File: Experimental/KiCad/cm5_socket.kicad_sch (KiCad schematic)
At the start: 23 parts, among them Q1 2N7002, X1 1-2199230-6

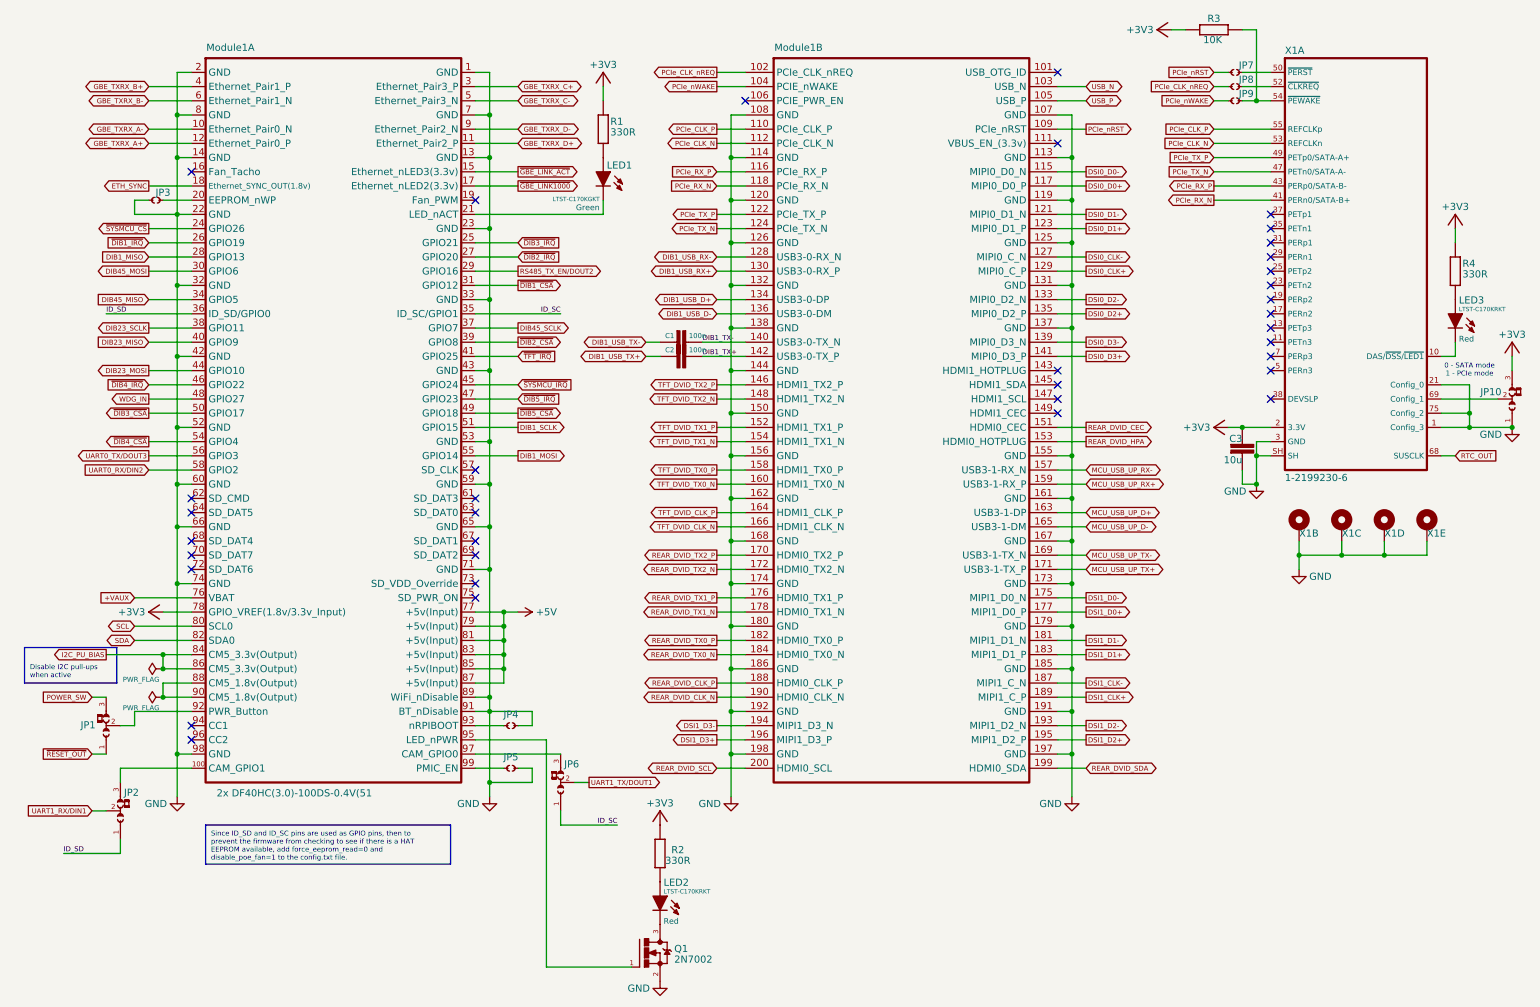
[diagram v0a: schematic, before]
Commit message: BOM update, small changes
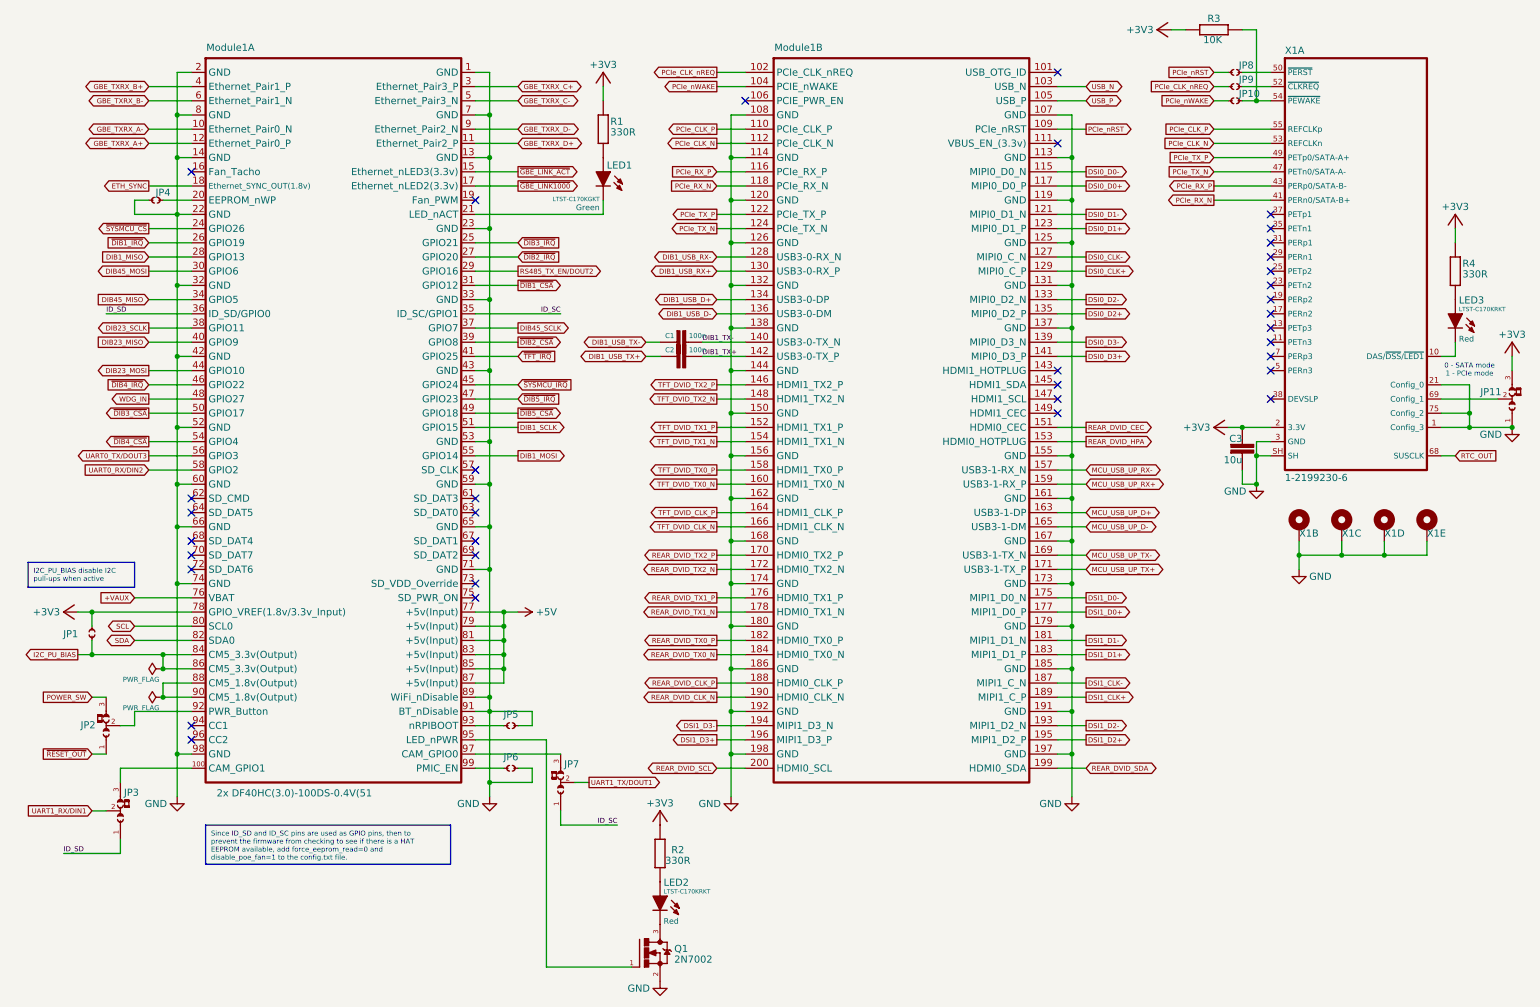
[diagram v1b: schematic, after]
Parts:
- added JP1: ~, PCM_EEZ_connectors:M22-2010246, symbol PCM_EEZ_unsorted:JP2 open
- renumbered JP9 to JP10, JP10 to JP11, JP1 to JP2, JP2 to JP3, JP3 to JP4, JP4 to JP5, JP5 to JP6, JP6 to JP7, JP7 to JP8, JP8 to JP9
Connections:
- net +3V3: now also JP1.2
- net I2C_PU_BIAS: now also JP1.1
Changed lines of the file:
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@@
 	(title_block
 		(title "BB3+ test mainboard")
-		(date "2025-10-11")
+		(date "2025-10-12")
 		(rev "r1B1")
 		(company "Envox d.o.o.")
@@
 		)
 	)
-	(text_box "Disable I2C pull-ups\nwhen active"
+	(text_box "I2C_PU_BIAS disable I2C\npull-ups when active"
 		(exclude_from_sim no)
-		(at 13.335 130.81 0)
-		(size 16.51 6.35)
+		(at 13.97 115.57 0)
+		(size 19.05 4.445)
 		(margins 0.9525 0.9525 0.9525 0.9525)
 		(stroke
@@
 				(color 132 0 132 1)
 			)
-			(justify left bottom)
+			(justify left top)
 		)
 	)
@@
 	)
 	(junction
+		(at 25.4 124.46)
+		(diameter 0)
+		(color 0 0 0 0)
+	)
+	(junction
 		(at 40.64 66.04)
 		(diameter 0)
@@
 	)
 	(junction
+		(at 25.4 132.08)
+		(diameter 0)
+		(color 0 0 0 0)
+	)
+	(junction
 		(at 99.06 134.62)
 		(diameter 0)
@@
 	(wire
 		(pts
+			(xy 25.4 129.54) (xy 25.4 132.08)
+		)
+		(stroke
+			(width 0)
+			(type default)
+		)
+	)
+	(wire
+		(pts
 			(xy 266.7 86.36) (xy 276.86 86.36)
 		)
@@
 	(wire
 		(pts
+			(xy 25.4 124.46) (xy 25.4 127)
+		)
+		(stroke
+			(width 0)
+			(type default)
+		)
+	)
+	(wire
+		(pts
 			(xy 25.4 139.7) (xy 27.94 139.7)
 		)
@@
 	(wire
 		(pts
-			(xy 38.1 124.46) (xy 43.18 124.46)
+			(xy 22.86 124.46) (xy 25.4 124.46)
 		)
 		(stroke
@@
 	(wire
 		(pts
+			(xy 25.4 124.46) (xy 43.18 124.46)
+		)
+		(stroke
+			(width 0)
+			(type default)
+		)
+	)
+	(wire
+		(pts
 			(xy 35.56 93.98) (xy 43.18 93.98)
 		)
@@
 	(wire
 		(pts
+			(xy 25.4 132.08) (xy 38.1 132.08)
+		)
+		(stroke
+			(width 0)
+			(type default)
+		)
+	)
+	(wire
+		(pts
 			(xy 40.64 66.04) (xy 43.18 66.04)
 		)
@@
 	(wire
 		(pts
-			(xy 27.94 132.08) (xy 38.1 132.08)
+			(xy 22.86 132.08) (xy 25.4 132.08)
 		)
 		(stroke
@@
 	(global_label "I2C_PU_BIAS"
 		(shape output)
-		(at 27.94 132.08 180)
+		(at 22.86 132.08 180)
 		(fields_autoplaced yes)
 		(effects
@@
 		)
 		(property "Intersheetrefs" "${INTERSHEET_REFS}"
-			(at 18.0535 132.08 0)
+			(at 12.9735 132.08 0)
 			(effects
 				(font
@@
 		(on_board yes)
 		(dnp no)
-		(property "Reference" "JP1"
+		(property "Reference" "JP2"
 			(at 26.035 145.415 90)
 			(effects
@@
 			(project "BB3plus MCU test board"
 				(path "/1df84e4f-233a-4f72-9418-c0020706bb76/d74ad35b-5ae5-4e4c-8cd2-c11fba35596b"
-					(reference "JP1")
+					(reference "JP2")
 					(unit 1)
 				)
@@
 	)
 	(symbol
+		(lib_id "PCM_EEZ_unsorted:JP2 open")
+		(at 25.4 129.54 90)
+		(unit 1)
+		(exclude_from_sim no)
+		(in_bom no)
+		(on_board yes)
+		(dnp no)
+		(property "Reference" "JP1"
+			(at 21.59 127.635 90)
+			(effects
+				(font
+					(size 1.27 1.27)
+				)
+				(justify bottom)
+			)
+		)
+		(property "Value" "~"
+			(at 25.4 129.54 0)
+			(effects
+				(font
+					(size 1.27 1.27)
+				)
+				(hide yes)
+			)
+		)
+		(property "Footprint" "PCM_EEZ_connectors:M22-2010246"
+			(at 27.94 129.54 0)
+			(effects
+				(font
+					(size 1.27 1.27)
+				)
+				(hide yes)
+			)
+		)
+		(property "Datasheet" ""
+			(at 25.4 129.54 0)
+			(effects
+				(font
+					(size 1.27 1.27)
+				)
+				(hide yes)
+			)
+		)
+		(property "Description" ""
+			(at 25.4 129.54 0)
+			(effects
+				(font
+					(size 1.27 1.27)
+				)
+				(hide yes)
+			)
+		)
+		(property "DigiKey" ""
+			(at 25.4 129.54 0)
+			(effects
+				(font
+					(size 1.27 1.27)
+				)
+				(hide yes)
+			)
+		)
+		(property "Mouser" ""
+			(at 25.4 129.54 0)
+			(effects
+				(font
+					(size 1.27 1.27)
+				)
+				(hide yes)
+			)
+		)
+		(property "TME" ""
+			(at 25.4 129.54 0)
+			(effects
+				(font
+					(size 1.27 1.27)
+				)
+				(hide yes)
+			)
+		)
+		(property "LCSC" ""
+			(at 25.4 129.54 0)
+			(effects
+				(font
+					(size 1.27 1.27)
+				)
+				(hide yes)
+			)
+		)
+		(property "Label" "LEGACY 3V3"
+			(at 25.4 129.54 0)
+			(effects
+				(font
+					(size 0.889 0.889)
+				)
+				(hide yes)
+			)
+		)
+		(pin "1"
+		)
+		(pin "2"
+		)
+		(instances
+			(project "BB3plus test mainboard"
+				(path "/1df84e4f-233a-4f72-9418-c0020706bb76/d74ad35b-5ae5-4e4c-8cd2-c11fba35596b"
+					(reference "JP1")
+					(unit 1)
+				)
+			)
+		)
+	)
+	(symbol
 		(lib_id "PCM_EEZ_connectors:Bus_M.2_Socket (with holes) 80 mm")
 		(at 256.54 111.76 0)
@@
 		(on_board yes)
 		(dnp no)
-		(property "Reference" "JP3"
+		(property "Reference" "JP4"
 			(at 38.1 50.165 0)
 			(effects
@@
 			(project ""
 				(path "/1df84e4f-233a-4f72-9418-c0020706bb76/d74ad35b-5ae5-4e4c-8cd2-c11fba35596b"
-					(reference "JP3")
+					(reference "JP4")
 					(unit 1)
 				)
@@
 		(on_board yes)
 		(dnp no)
-		(property "Reference" "JP5"
+		(property "Reference" "JP6"
 			(at 100.33 151.13 0)
 			(effects
@@
 			(project "BB3plus MCU test board"
 				(path "/1df84e4f-233a-4f72-9418-c0020706bb76/d74ad35b-5ae5-4e4c-8cd2-c11fba35596b"
-					(reference "JP5")
+					(reference "JP6")
 					(unit 1)
 				)
@@
 		(on_board yes)
 		(dnp no)
-		(property "Reference" "JP2"
+		(property "Reference" "JP3"
 			(at 31.115 157.48 90)
 			(effects
@@
 			(project "BB3plus MCU test board"
 				(path "/1df84e4f-233a-4f72-9418-c0020706bb76/d74ad35b-5ae5-4e4c-8cd2-c11fba35596b"
-					(reference "JP2")
+					(reference "JP3")
 					(unit 1)
 				)
@@
 		(on_board yes)
 		(dnp no)
-		(property "Reference" "JP6"
+		(property "Reference" "JP7"
 			(at 109.855 152.4 90)
 			(effects
@@
 			(project "BB3plus MCU test board"
 				(path "/1df84e4f-233a-4f72-9418-c0020706bb76/d74ad35b-5ae5-4e4c-8cd2-c11fba35596b"
-					(reference "JP6")
+					(reference "JP7")
 					(unit 1)
 				)
@@
 		(on_board yes)
 		(dnp no)
-		(property "Reference" "JP4"
+		(property "Reference" "JP5"
 			(at 100.33 143.51 0)
 			(effects
@@
 			(project "BB3plus MCU test board"
 				(path "/1df84e4f-233a-4f72-9418-c0020706bb76/d74ad35b-5ae5-4e4c-8cd2-c11fba35596b"
-					(reference "JP4")
+					(reference "JP5")
 					(unit 1)
 				)
@@
 		(on_board yes)
 		(dnp no)
-		(property "Reference" "JP7"
+		(property "Reference" "JP8"
 			(at 230.505 26.67 0)
 			(effects
@@
 			(project ""
 				(path "/1df84e4f-233a-4f72-9418-c0020706bb76/d74ad35b-5ae5-4e4c-8cd2-c11fba35596b"
-					(reference "JP7")
+					(reference "JP8")
 					(unit 1)
 				)
@@
 		(on_board yes)
 		(dnp no)
-		(property "Reference" "JP10"
+		(property "Reference" "JP11"
 			(at 277.495 85.09 90)
 			(effects
@@
 			(project ""
 				(path "/1df84e4f-233a-4f72-9418-c0020706bb76/d74ad35b-5ae5-4e4c-8cd2-c11fba35596b"
-					(reference "JP10")
+					(reference "JP11")
 					(unit 1)
 				)
@@
 	(symbol
 		(lib_id "PCM_EEZ_symbols:+3V3")
-		(at 35.56 124.46 90)
+		(at 20.32 124.46 90)
 		(mirror x)
 		(unit 1)
@@
 		(dnp no)
 		(property "Reference" "#+3V01"
-			(at 35.56 124.46 0)
+			(at 20.32 124.46 0)
 			(effects
 				(font
@@
 		)
 		(property "Value" "+3V3"
-			(at 34.925 124.46 90)
+			(at 19.685 124.46 90)
 			(effects
 				(font
@@
 		)
 		(property "Footprint" ""
-			(at 35.56 124.46 0)
+			(at 20.32 124.46 0)
 			(effects
 				(font
@@
 		)
 		(property "Datasheet" ""
-			(at 35.56 124.46 0)
+			(at 20.32 124.46 0)
 			(effects
 				(font
@@
 		)
 		(property "Description" ""
-			(at 35.56 124.46 0)
+			(at 20.32 124.46 0)
 			(effects
 				(font
@@
 		(on_board yes)
 		(dnp no)
-		(property "Reference" "JP8"
+		(property "Reference" "JP9"
 			(at 230.505 29.21 0)
 			(effects
@@
 			(project "BB3plus MCU test board"
 				(path "/1df84e4f-233a-4f72-9418-c0020706bb76/d74ad35b-5ae5-4e4c-8cd2-c11fba35596b"
-					(reference "JP8")
+					(reference "JP9")
 					(unit 1)
 				)
@@
 		(on_board yes)
 		(dnp no)
-		(property "Reference" "JP9"
+		(property "Reference" "JP10"
 			(at 230.505 31.75 0)
 			(effects
@@
 			(project "BB3plus MCU test board"
 				(path "/1df84e4f-233a-4f72-9418-c0020706bb76/d74ad35b-5ae5-4e4c-8cd2-c11fba35596b"
-					(reference "JP9")
+					(reference "JP10")
 					(unit 1)
 				)

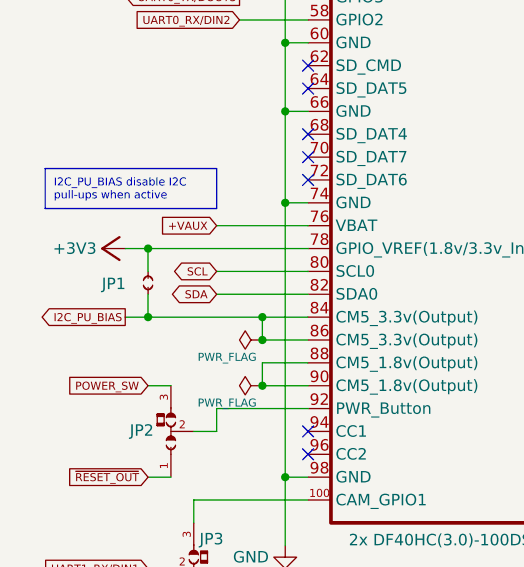
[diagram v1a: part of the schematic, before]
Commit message: AC/DC module replaced with 45/60W model
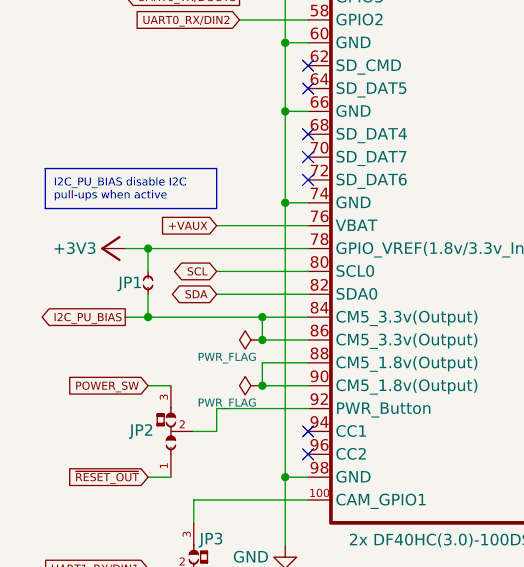
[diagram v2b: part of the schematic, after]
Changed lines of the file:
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@@
 		(dnp no)
 		(property "Reference" "JP1"
-			(at 21.59 127.635 90)
+			(at 24.765 128.27 90)
 			(effects
 				(font
 					(size 1.27 1.27)
 				)
-				(justify bottom)
+				(justify left)
 			)
 		)

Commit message: Update project info
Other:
- company: Envox d.o.o. -> ${project_creator}
- title: BB3+ test mainboard -> ${project_name}
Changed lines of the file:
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@@
 	(paper "A4")
 	(title_block
-		(title "BB3+ test mainboard")
-		(date "2025-10-12")
-		(rev "r1B1")
-		(company "Envox d.o.o.")
-		(comment 1 "Licensed under the TAPR Open Hardware License (www.tapr.org/OHL)")
-		(comment 2 "More info at http://www.envox.eu/")
+		(title "${project_name}")
+		(date "2025-10-13")
+		(rev "${project_version}")
+		(company "${project_creator}")
+		(comment 1 "${project_license}")
+		(comment 2 "${project_info}")
 	)
 	(text "0 - SATA mode\n1 - PCIe mode"

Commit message: Various small fixes
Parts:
- Module1: symbol PCM_EEZ_connectors:Raspberry Pi CM5 -> PCM_EEZ_connectors:Raspberry Pi CM5 (MB)
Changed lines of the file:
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@@
 	)
 	(symbol
-		(lib_id "PCM_EEZ_connectors:Raspberry Pi CM5")
+		(lib_id "PCM_EEZ_connectors:Raspberry Pi CM5 (MB)")
 		(at 45.72 25.4 0)
 		(unit 1)
@@
 	)
 	(symbol
-		(lib_id "PCM_EEZ_connectors:Raspberry Pi CM5")
+		(lib_id "PCM_EEZ_connectors:Raspberry Pi CM5 (MB)")
 		(at 147.32 25.4 0)
 		(unit 2)
